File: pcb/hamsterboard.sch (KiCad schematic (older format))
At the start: 1 part

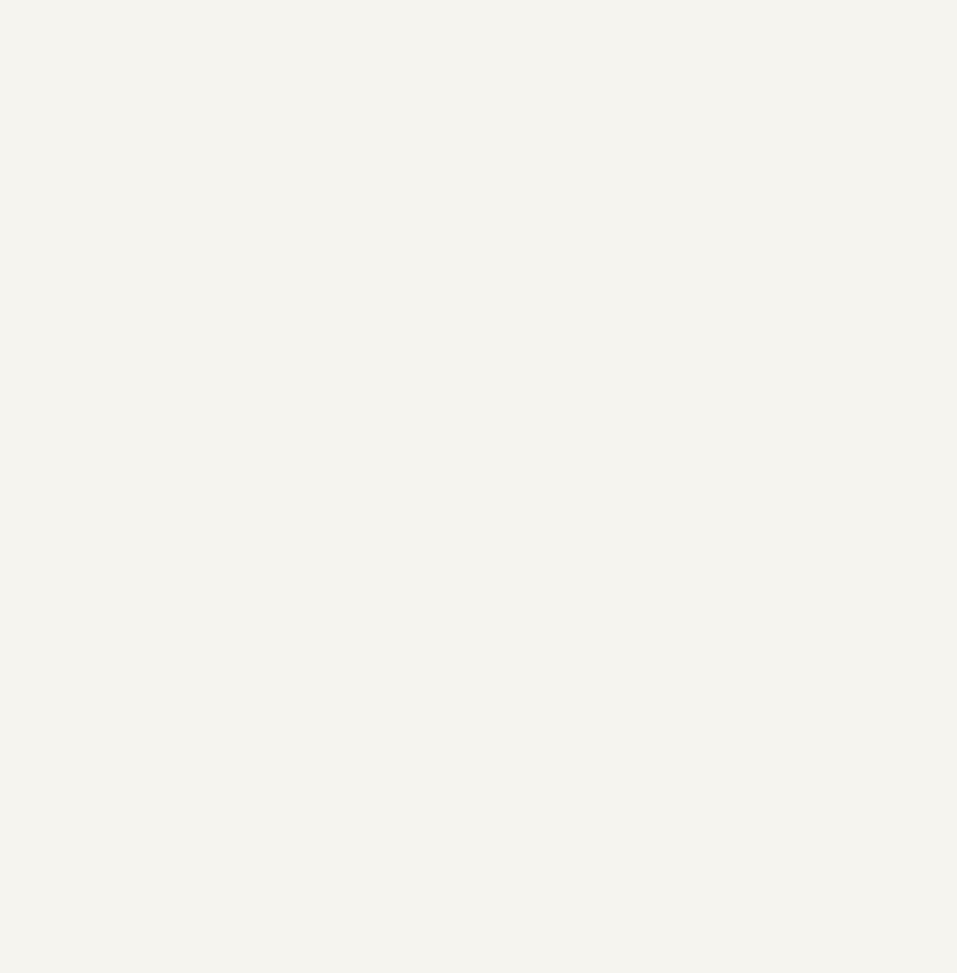
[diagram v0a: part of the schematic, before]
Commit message: Add dsPIC33EP256GP506 to lib
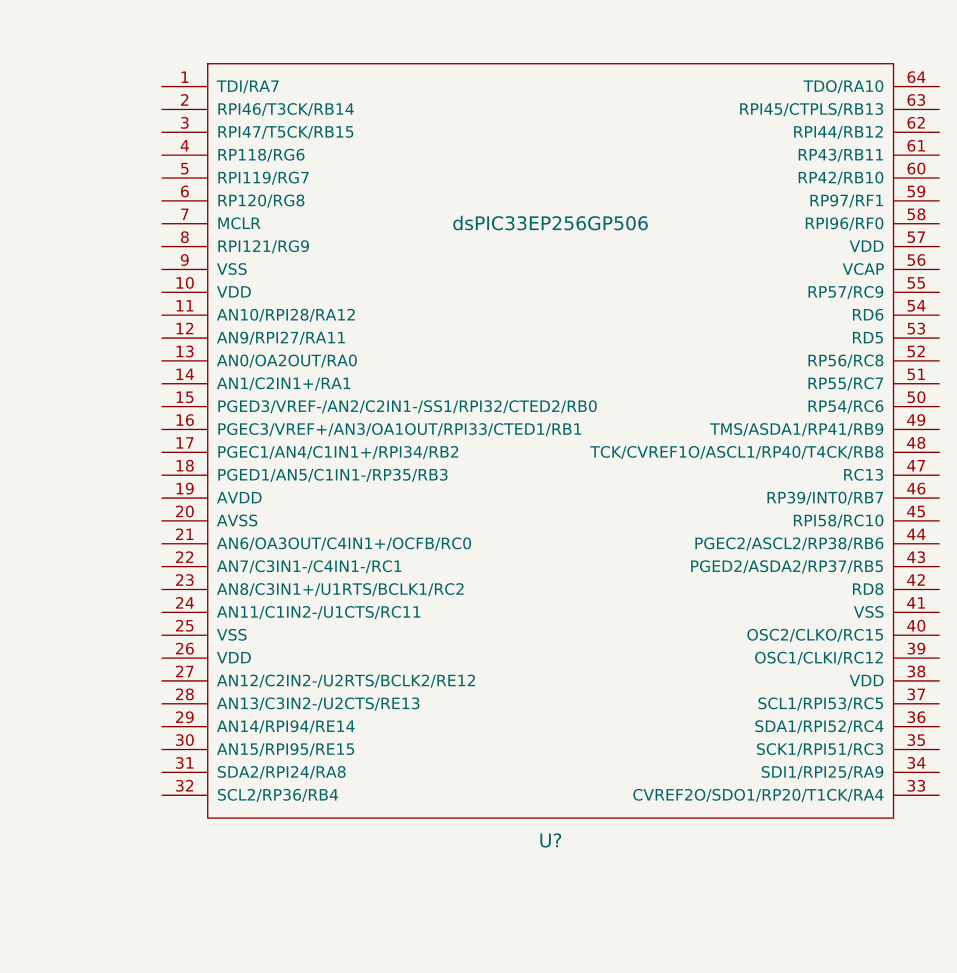
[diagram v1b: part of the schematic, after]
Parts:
- added U?: dsPIC33EP256GP506, symbol dsPIC33EP256GP506
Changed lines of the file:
@@
 LIBS:valves
 LIBS:hamsterboard
+LIBS:hamsterboard-cache
 EELAYER 25 0
 EELAYER END
@@
 	1    0    0    -1
 $EndComp
+$Comp
+L dsPIC33EP256GP506 U?
+U 1 1 5A870EB3
+P 5950 2550
+F 0 "U?" H 5950 800 60  0000 C CNN
+F 1 "dsPIC33EP256GP506" H 5950 3500 60  0000 C CNN
+F 2 "" H 4800 2000 60  0001 C CNN
+F 3 "" H 4800 2000 60  0001 C CNN
+	1    5950 2550
+	1    0    0    -1
+$EndComp

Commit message: hamsterboard.sch
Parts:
- added C? (x2): C_Small, symbol C_Small
- added C? (x2): 27p, symbol C_Small
- added C? (x2): 100n, symbol C_Small
- added J?: USB_OTG, symbol USB_OTG
- added L? (x2): L, symbol L
- added R?: 0, symbol R_Small
- added R?: 12k, symbol R_Small
- added R?: 1k, symbol R_Small
- added U?: AP1117-33, TO_SOT_Packages_SMD:SOT-223-3Lead_TabPin2, symbol AP1117-33
- added Y1: 12 Mhz, symbol Crystal
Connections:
- net Earth: now reaches IC?.1 (GND)
- net Earth: now also IC?.10 (AGND), IC?.11 (GND), IC?.13 (TEST), IC?.15 (GND), IC?.25 (GND), IC?.35 (GND), IC?.47 (GND), IC?.5 (GND), IC?.51 (GND), C?.2, C?.2, C?.2, C?.2, C?.2, C?.2, J?.5 (GND), R?.2, R?.2, U?.1 (GND)
- net at IC?.14 (RESET#): now also R?.1
- net at IC?.2 (OSCI): now also C?.1, Y1.2
- net at IC?.3 (OSCO): now also C?.1, Y1.1
- net VPHY: now reaches IC?.4 (VPHY)
- net VPHY: now also C?.1
- net +3V3: now reaches IC?.50 (VREGIN)
- net +3V3: now also C?.1, L?.2, L?.2, R?.2, U?.2 (VO)
- net at IC?.6 (REF): now also R?.1
- net at IC?.7 (DM): now also J?.3 (D+)
- net at IC?.8 (DP): now also J?.2 (D-)
- net VPLL: now reaches IC?.9 (VPLL)
- net VPLL: now also C?.1, L?.1
- new net: C?.1, J?.1 (VBUS), U?.3 (VI)
- new net: J?.6 (Shield), R?.1
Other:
- moved on the sheet: IC?, U?
